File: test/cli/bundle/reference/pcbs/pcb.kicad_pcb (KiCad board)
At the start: 2 copper layers, 18 x 18 mm, 1 part

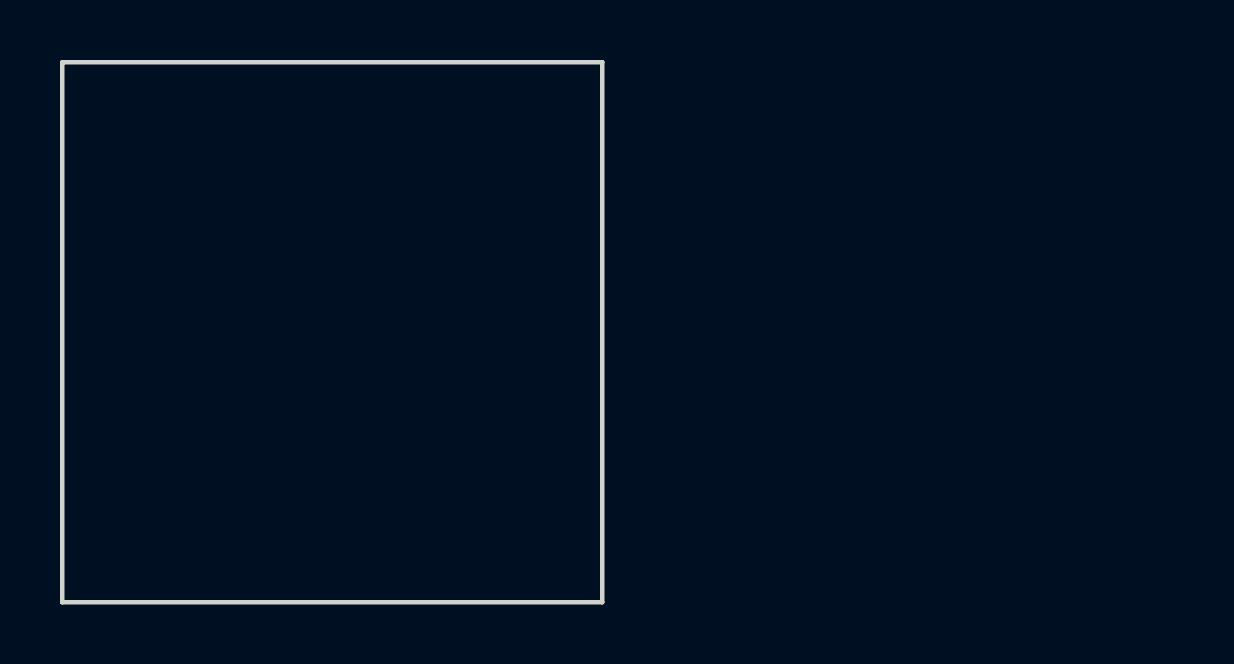
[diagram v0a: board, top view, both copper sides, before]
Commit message: Fix tests and add coverage for injected outlines
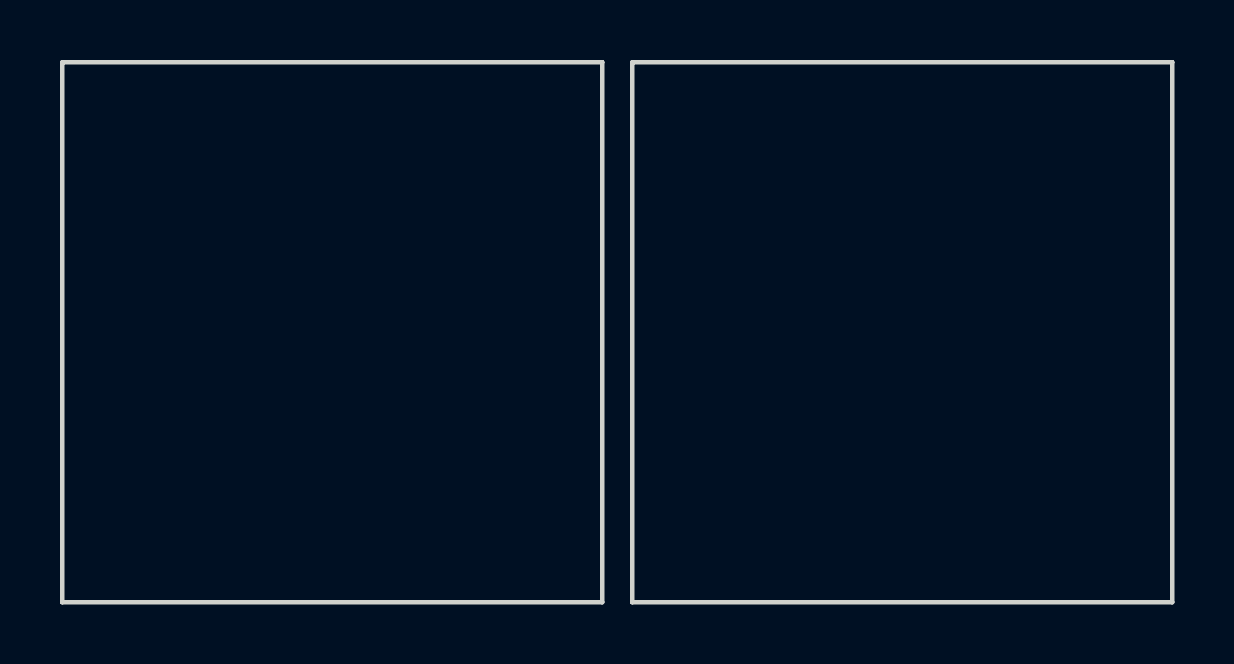
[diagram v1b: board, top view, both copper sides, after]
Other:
- board size 18 x 18 mm -> 37 x 18 mm
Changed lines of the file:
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@@
 (gr_line (start 9 -9) (end -9 -9) (angle 90) (layer Edge.Cuts) (width 0.15))
 (gr_line (start -9 -9) (end -9 9) (angle 90) (layer Edge.Cuts) (width 0.15))
+(gr_line (start 10 9) (end 28 9) (angle 90) (layer Edge.Cuts) (width 0.15))
+(gr_line (start 28 9) (end 28 -9) (angle 90) (layer Edge.Cuts) (width 0.15))
+(gr_line (start 28 -9) (end 10 -9) (angle 90) (layer Edge.Cuts) (width 0.15))
+(gr_line (start 10 -9) (end 10 9) (angle 90) (layer Edge.Cuts) (width 0.15))
 )
